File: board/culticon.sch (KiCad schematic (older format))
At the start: 32 parts

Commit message: minimal working schem
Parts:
- removed R?: R, symbol Device:R
- added C? (x3): C, symbol Device:C
- added J?: Conn_01x02, symbol Connector_Generic:Conn_01x02
- added J?: Conn_01x04, symbol Connector_Generic:Conn_01x04
- added Q?: BT136-500, Package_TO_SOT_THT:TO-220-3_Vertical, symbol Triac_Thyristor:BT136-500
- added R? (x9): R, symbol Device:R
- added U?: MOC3021M, symbol Relay_SolidState:MOC3021M
- added U?: 24LC64, symbol Memory_EEPROM:24LC64
- added U? (x2): PC817, Package_DIP:DIP-4_W7.62mm, symbol Isolator:PC817
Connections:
- net labels added: eeprom_wp, i2c_scl, i2c_sda, relay_t, sqw_out, sync_pulse, triac1_t, triac2_t, uart_rx, uart_tx
- wire segments 118 -> 201
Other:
- moved on the sheet: C?, D?, J?, K?, Q?, R?, T?, U?, Y?

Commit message: complete dev schem
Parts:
- removed C?: C, symbol Device:C
- removed R?: R, symbol Device:R
- added C?: CP, symbol Device:CP
- added R? (x9): R, symbol Device:R
- added R?: LDR, symbol Device:R_PHOTO
- added RV?: R_POT_TRIM, symbol Device:R_POT_TRIM
- added SW? (x4): SW_SPST, symbol Switch:SW_SPST
- added TH?: NTC_5K, symbol Device:Thermistor_NTC
- added U?: RC1602A, Display:RC1602A, symbol Display_Character:RC1602A
- added U?: 24LC64, symbol Memory_EEPROM:24LC64
- added U? (x2): DHT11, Sensor:Aosong_DHT11_5.5x12.0_P2.54mm, symbol Sensor:DHT11
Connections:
- net +5V: now also R?.2, R?.2, R?.2, R?.2, RV?.3, U?.1 (A0), U?.1 (VCC), U?.1 (VCC), U?.2 (VDD), U?.8 (VCC)
- net Earth: now also U?.7 (WP), R?.2, RV?.1, SW?.2 (B), SW?.2 (B), SW?.2 (B), SW?.2 (B), TH?.2, U?.1 (VSS), U?.10 (DB3), U?.16 (K), U?.2 (A1), U?.3 (A2), U?.4 (GND), U?.4 (GND), U?.4 (GND), U?.5 (R/W), U?.7 (DB0), U?.7 (WP), U?.8 (DB1), U?.9 (DB2)
- net i2c_scl: now also U?.6 (SCL)
- net i2c_sda: now also U?.5 (SDA)
- net at U?.11 (PD5): now also U?.2 (IO)
- net at U?.12 (PD6): now also U?.2 (IO)
- net lcd_e: now reaches U?.13 (PD7)
- net lcd_e: now also U?.6 (E)
- net at U?.14 (PB0): now also U?.4 (RS)
- net lcd_bl: now reaches U?.15 (PB1)
- net lcd_bl: now also U?.15 (A/VEE)
- net at U?.16 (PB2): now also U?.11 (DB4)
- net at U?.17 (PB3): now also U?.12 (DB5)
- net at U?.18 (PB4): now also U?.13 (DB6)
- net at U?.19 (PB5): now also U?.14 (DB7)
- net sw1_adc: now reaches U?.23 (PC0)
- net sw1_adc: now also R?.1, R?.2, R?.2
- net sw2_adc: now reaches U?.24 (PC1)
- net sw2_adc: now also R?.1, R?.2, R?.2
- net at U?.25 (PC2): now also R?.1, R?.1
- net at J?.4 (Pin_4), U?.3: now also U?.2, C?.2
- net at J?.2 (Pin_2), U?.4: now also R?.2
- net at U?.1: now also J?.3 (Pin_3); no longer J?.1 (Pin_1)
- net eeprom_wp: no longer names the net of U?.26 (PC3)
- net eeprom_wp: now also R?.1, TH?.1; no longer U?.7 (WP)
- net triac1_t: no longer names the net of R?.1, U?.9 (PB6/XTAL1)
- net triac2_t: no longer names the net of R?.1, U?.10 (PB7/XTAL2)
- new net: C?.1, J?.1 (Pin_1), R?.1
- new net: RV?.2, U?.3 (VO)
- new net: R?.1, SW?.1 (A) (x4)
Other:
- moved on the sheet: C?, D?, J?, K?, Q?, R?, U?

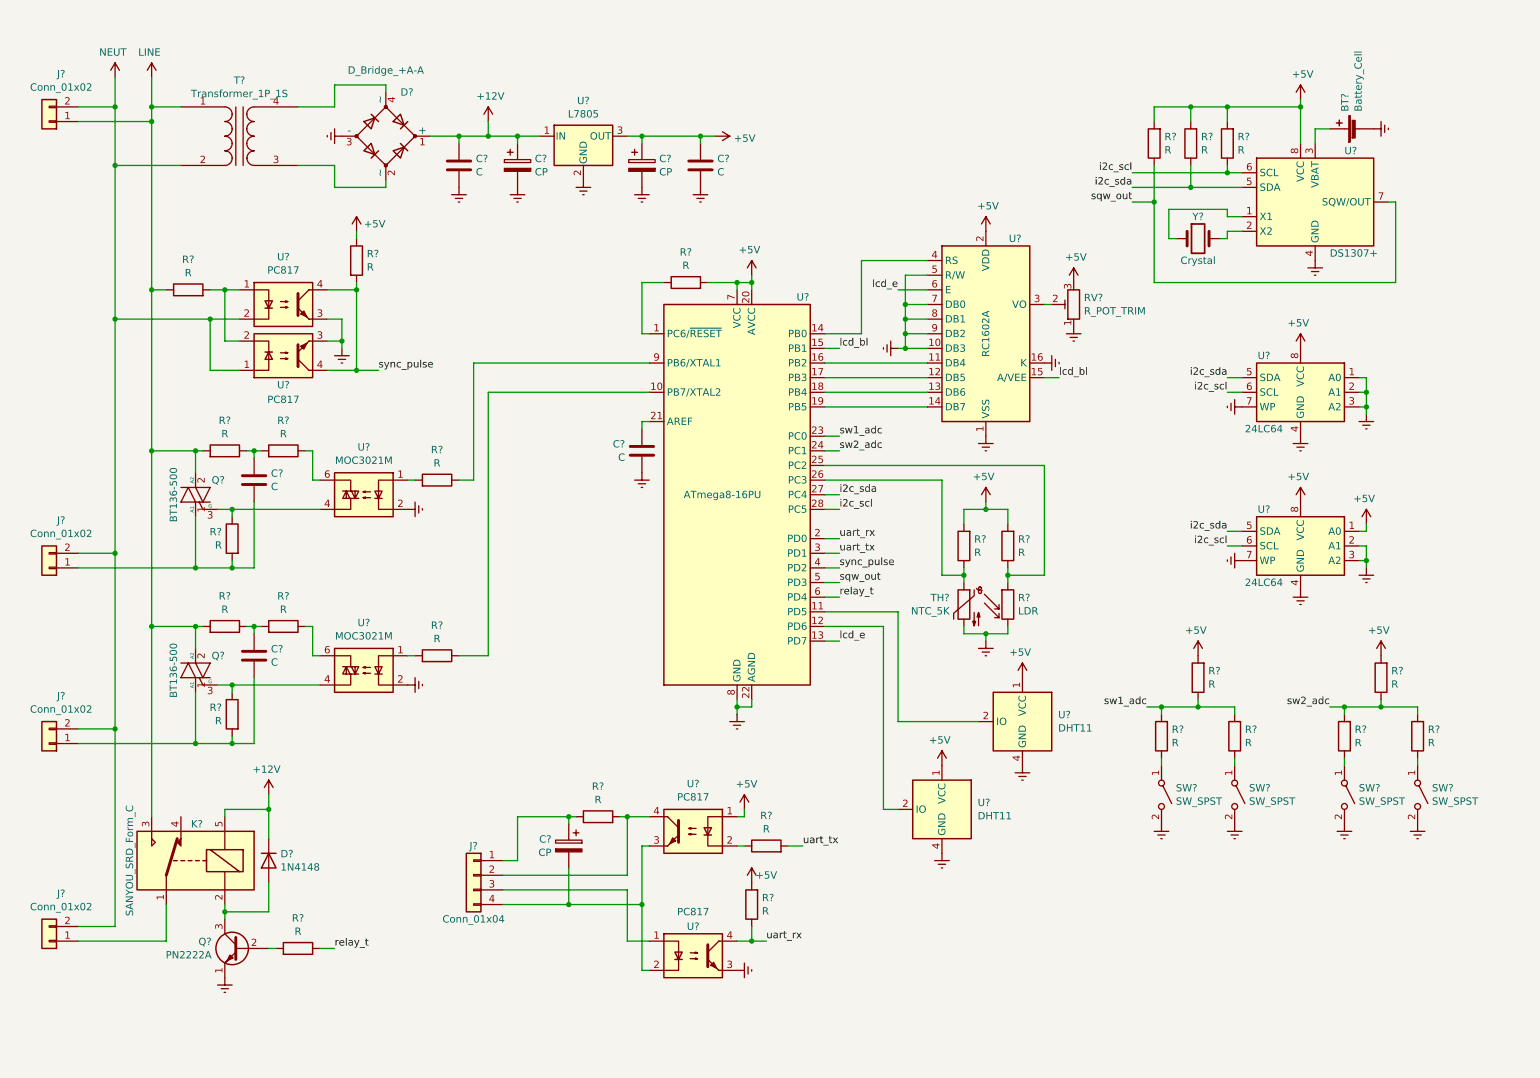
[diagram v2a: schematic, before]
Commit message: add comp refs & some values
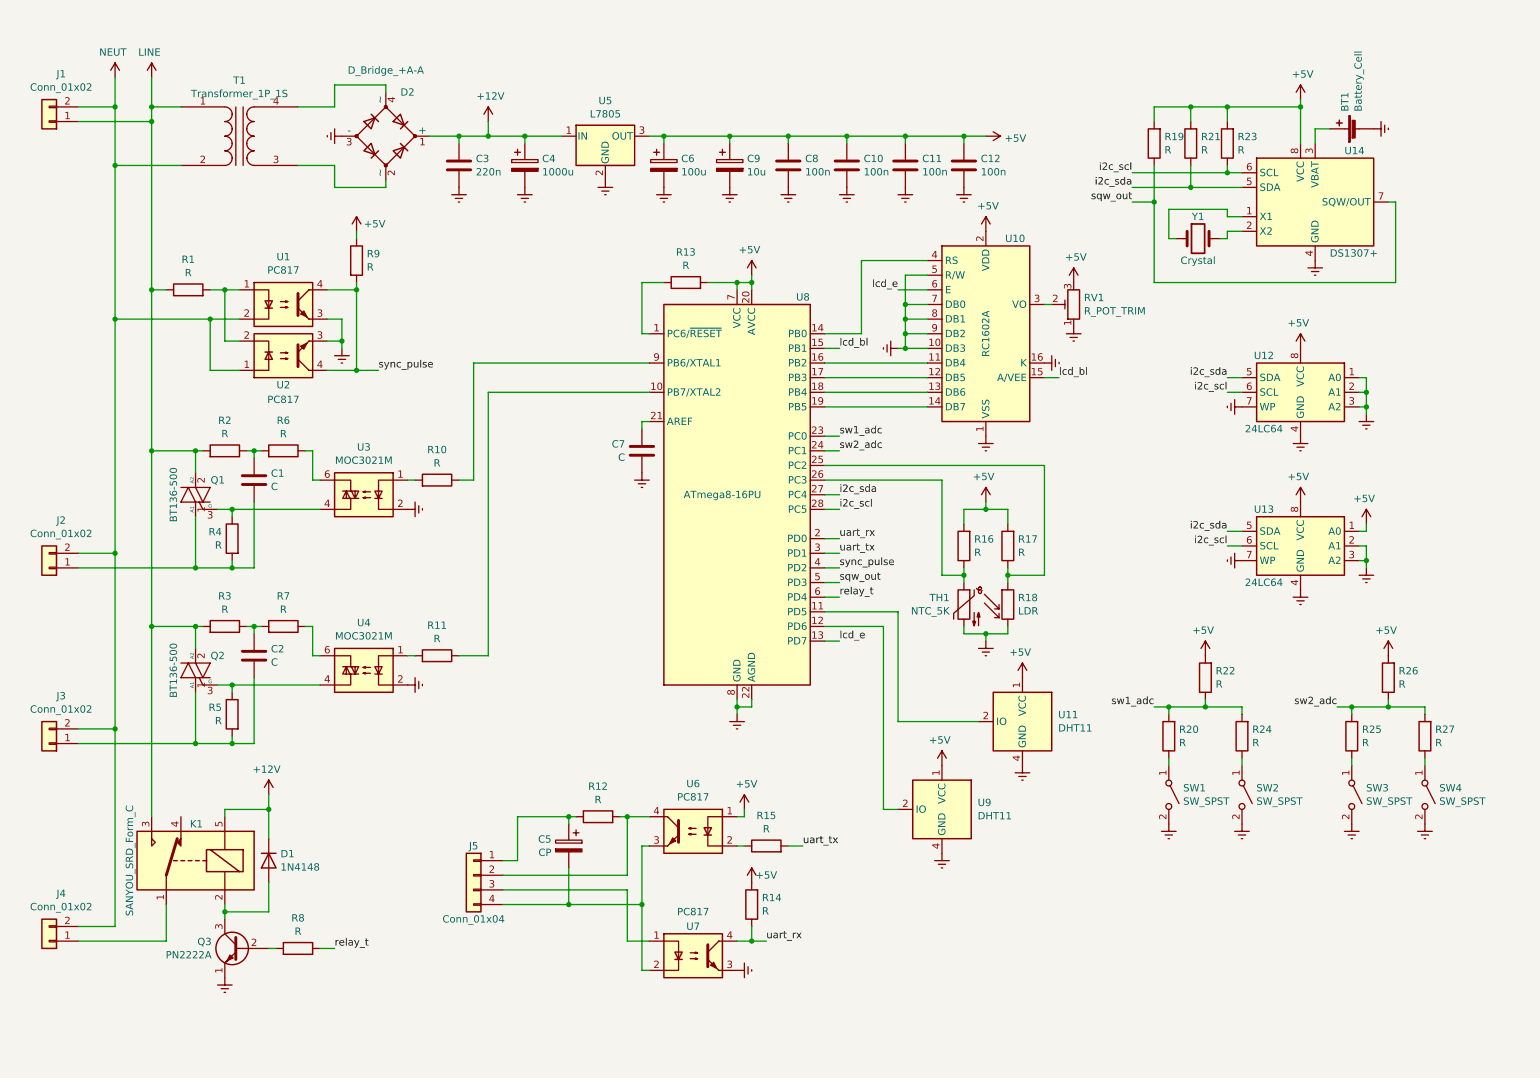
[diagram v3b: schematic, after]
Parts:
- added C10, C11, C12: 100n, symbol Device:C
- added C9: 10u, symbol Device:CP
- C3: renamed from C?; value C -> 220n
- C4: renamed from C?; value CP -> 1000u
- C6: renamed from C?; value CP -> 100u
- C8: renamed from C?; value C -> 100n
- gave numbers to parts that had none: 65
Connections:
- net +5V: now also C10.2, C11.2, C12.2, C9.1
- net Earth: now also C10.1, C11.1, C12.1, C9.2
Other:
- moved on the sheet: C4, C6, C8, R20, R22, R24, R25, R26, R27, SW1, SW2, SW3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

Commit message: some pin fixes
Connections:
- net relay_t: now also U8.5 (PD3); no longer U8.6 (PD4)
- net sqw_out: now also U8.4 (PD2); no longer U8.5 (PD3)
- net sync_pulse: now also U8.14 (PB0); no longer U8.4 (PD2)
- net at U8.11 (PD5): now also U9.2 (IO); no longer U11.2 (IO)
- net lcd_rs: now reaches U8.12 (PD6)
- net lcd_rs: now also U10.4 (RS); no longer U9.2 (IO)
- new net: U11.2 (IO), U8.6 (PD4)
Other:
- moved on the sheet: C10, C11, C12, C3, C4, C6, C8, C9, D2, J1, T1, U5

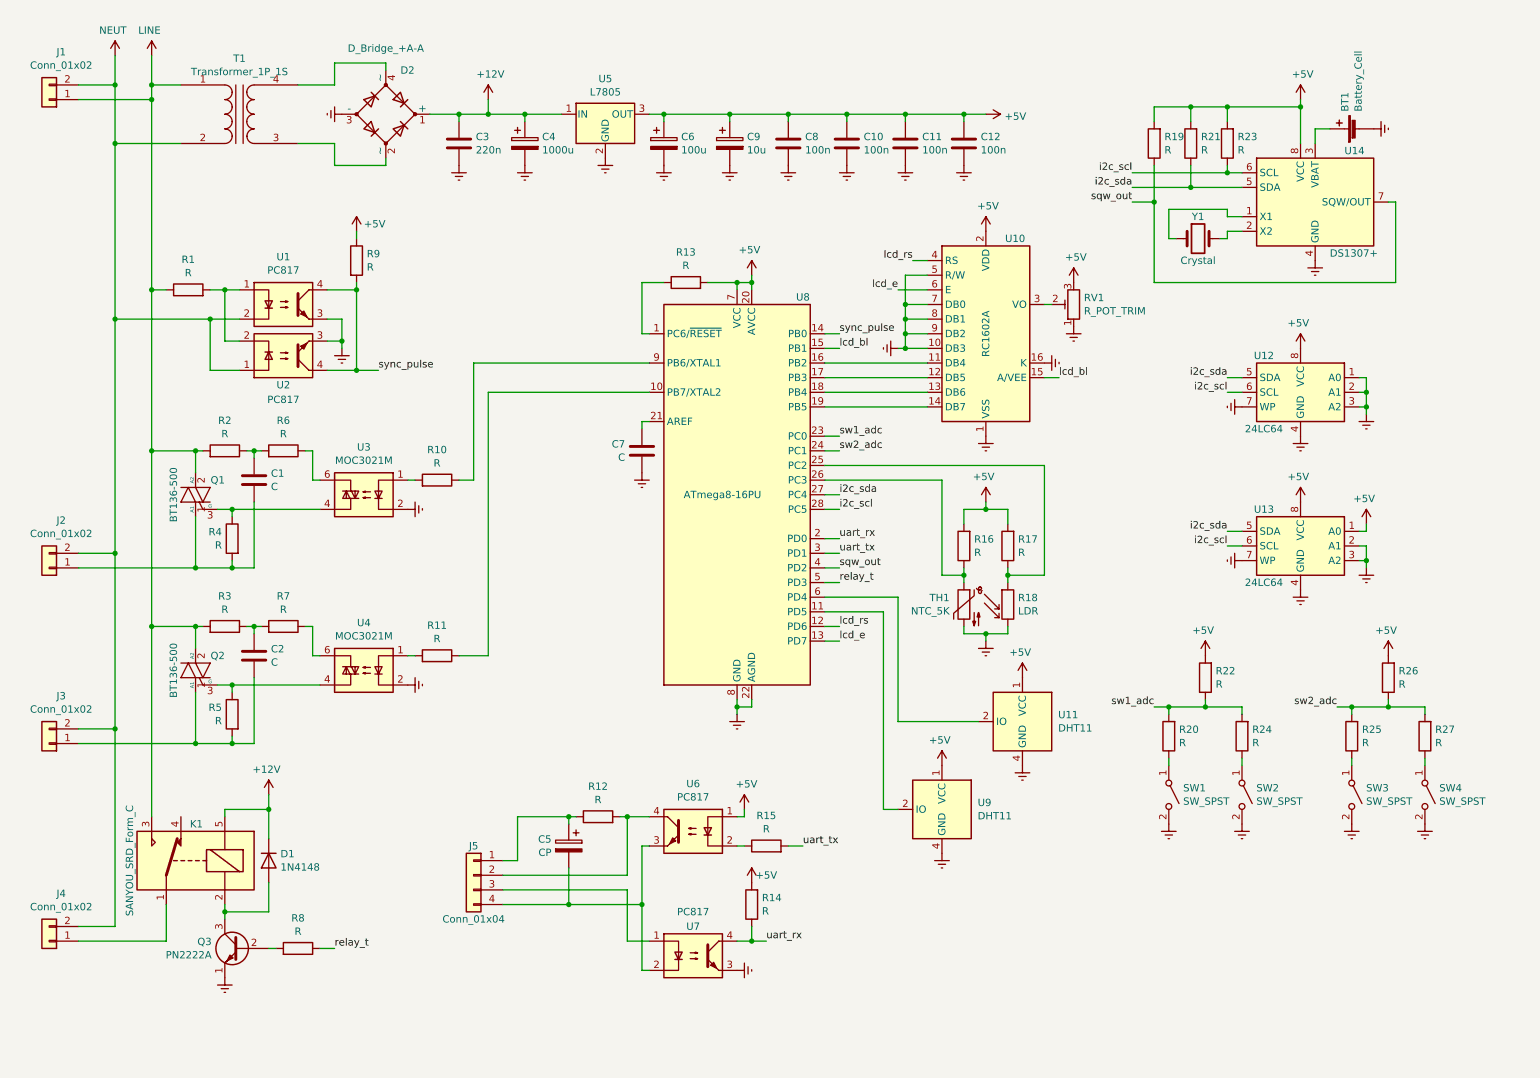
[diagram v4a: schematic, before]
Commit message: schem small fixes
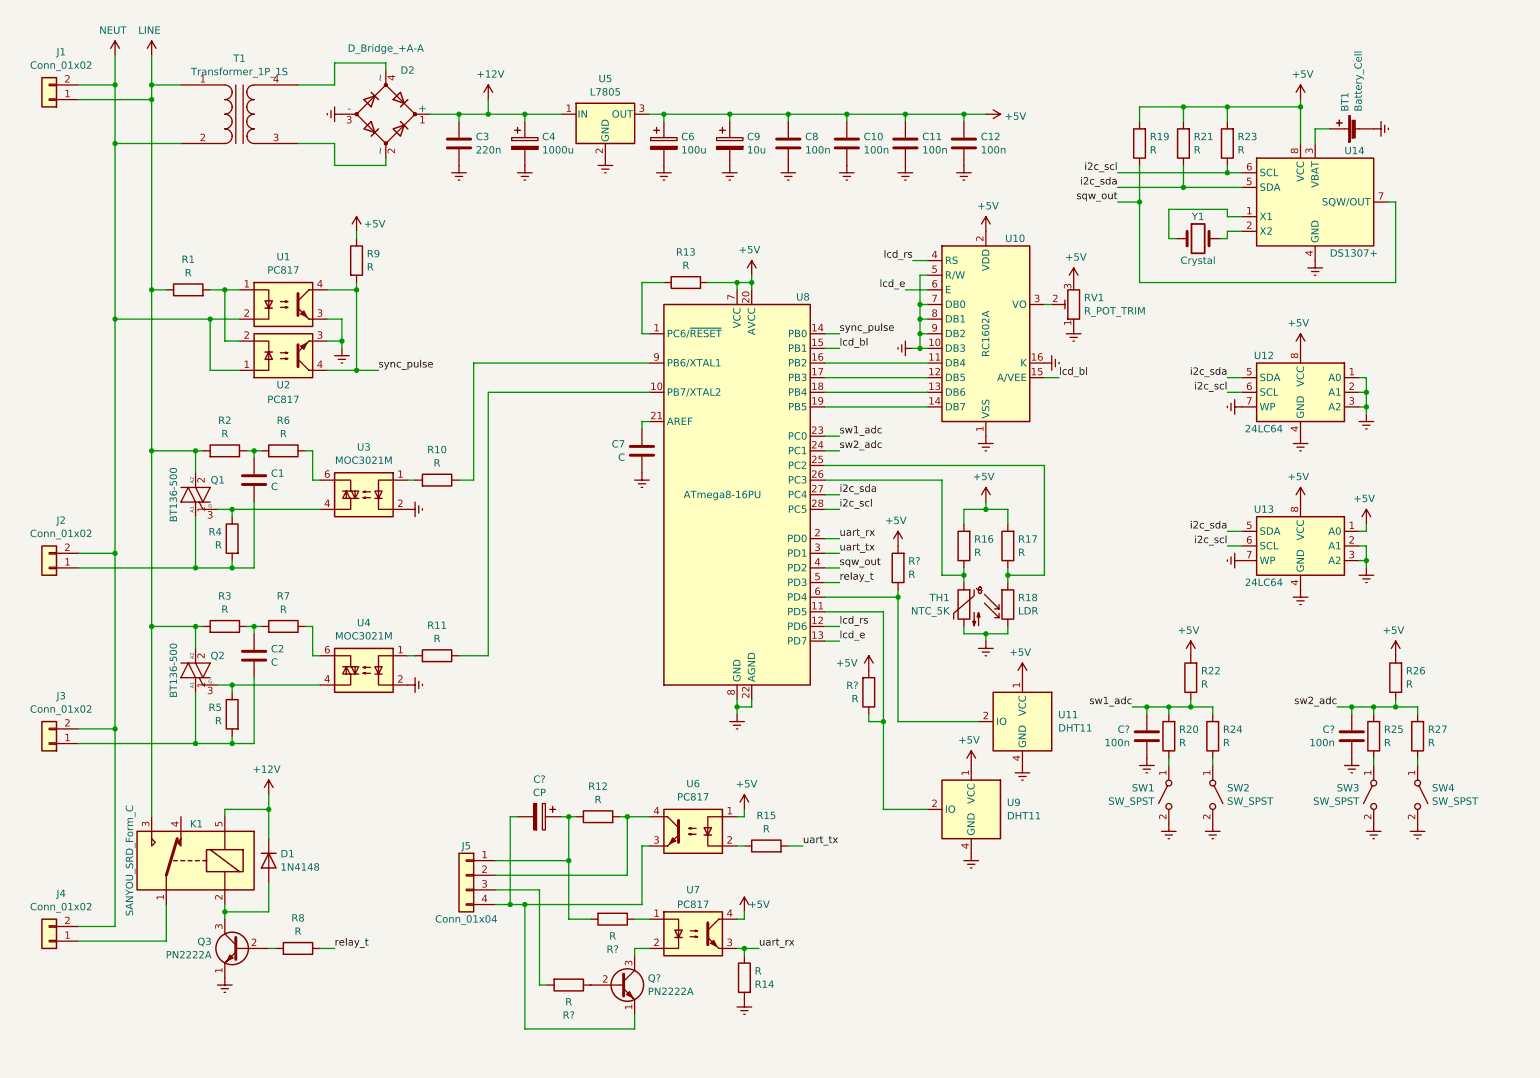
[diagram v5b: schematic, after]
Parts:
- removed C5: CP, symbol Device:CP
- added C? (x2): 100n, symbol Device:C
- added C?: CP, symbol Device:CP
- added Q?: PN2222A, Package_TO_SOT_THT:TO-92_Inline, symbol Transistor_BJT:PN2222A
- added R? (x4): R, symbol Device:R
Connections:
- net +5V: now also U7.4, R?.2, R?.2; no longer R14.2
- net Earth: now also R14.2, C?.1, C?.1; no longer U7.3
- net sw1_adc: now also C?.2
- net sw2_adc: now also C?.2
- net uart_rx: now also U7.3; no longer U7.4
- net at U8.11 (PD5), U9.2 (IO): now also R?.1
- net at U11.2 (IO), U8.6 (PD4): now also R?.1
- net at J5.4 (Pin_4), U6.3: now also C?.2, Q?.1 (E); no longer U7.2
- net at U7.1: now also R?.1; no longer J5.3 (Pin_3)
- net at J5.1 (Pin_1), R12.1: now also C?.1, R?.2
- new net: Q?.3 (C), U7.2
- new net: J5.3 (Pin_3), R?.2
- new net: Q?.2 (B), R?.1
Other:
- moved on the sheet: J5, R14, R19, R21, R22, R24, R25, R26, R27, SW1, SW2, SW3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
